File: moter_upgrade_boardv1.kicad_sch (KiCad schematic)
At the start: 54 parts, among them J2 Conn_01x03_Socket, J3 Conn_01x02_Socket, J4 Conn_01x02_Socket, J5 Conn_01x02_Socket, J6 Conn_01x02_Socket, J7 Conn_ST_STDC14, J8 Conn_01x05_Socket, J9 USB_C_Receptacle_USB2.0_16P, SW1 SW_SPDT, SW2 SW_Push, SW3 SW_Wuerth_450301014042, U1 BD33FC0FP, U2 TLP785, U3 TLP785, U4 STM32H523CCTx, U5 MCP2562-E-P, U6 CH340E, U7 BD33FC0FP

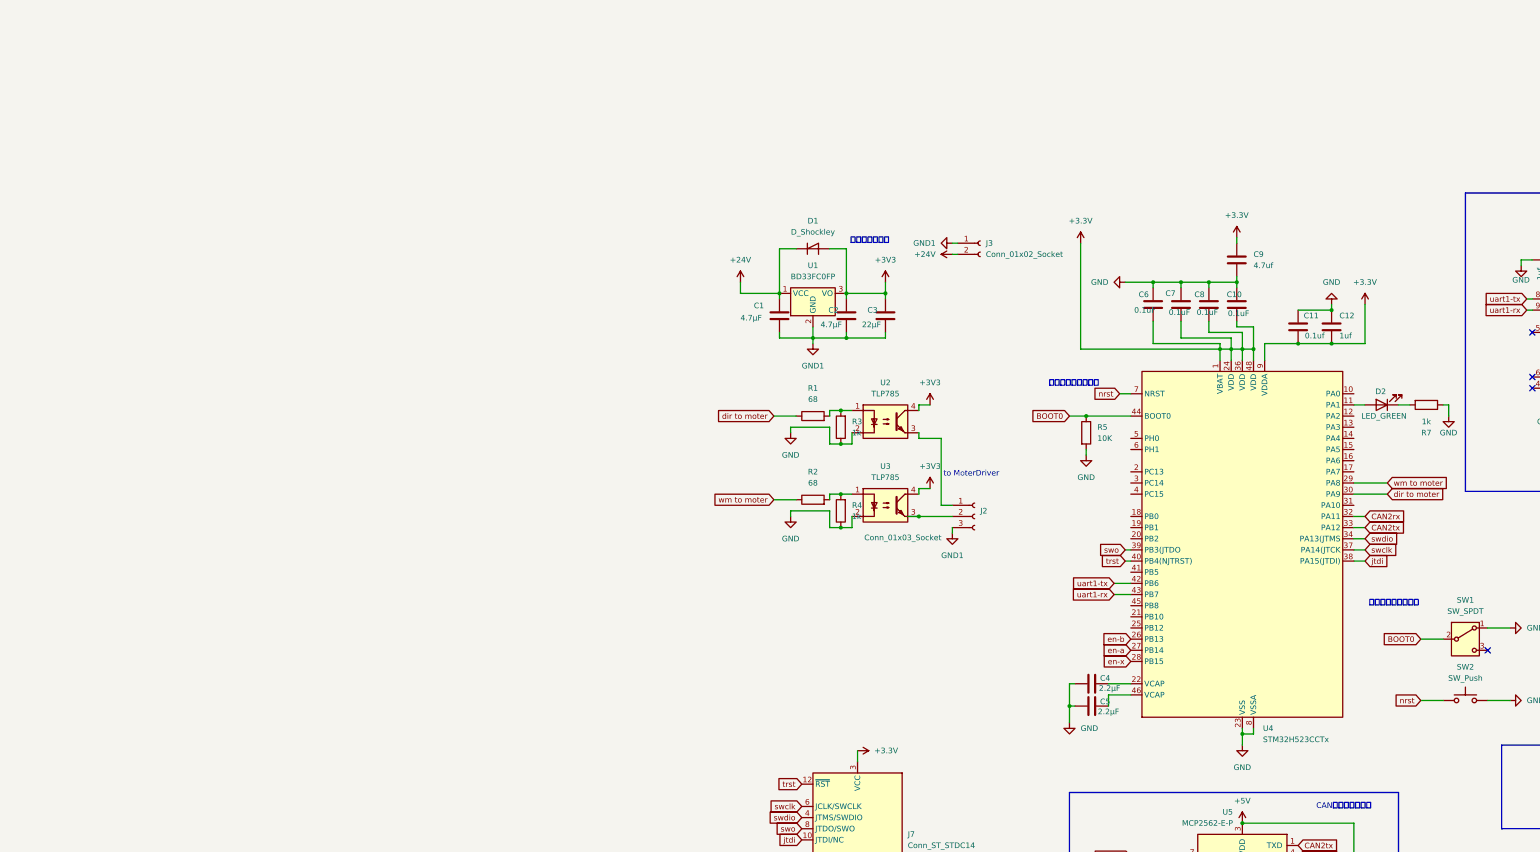
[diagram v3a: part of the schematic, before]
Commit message: マイコンの置き換え
stmH5からstmC5に置き換え(C5の中身はf446)
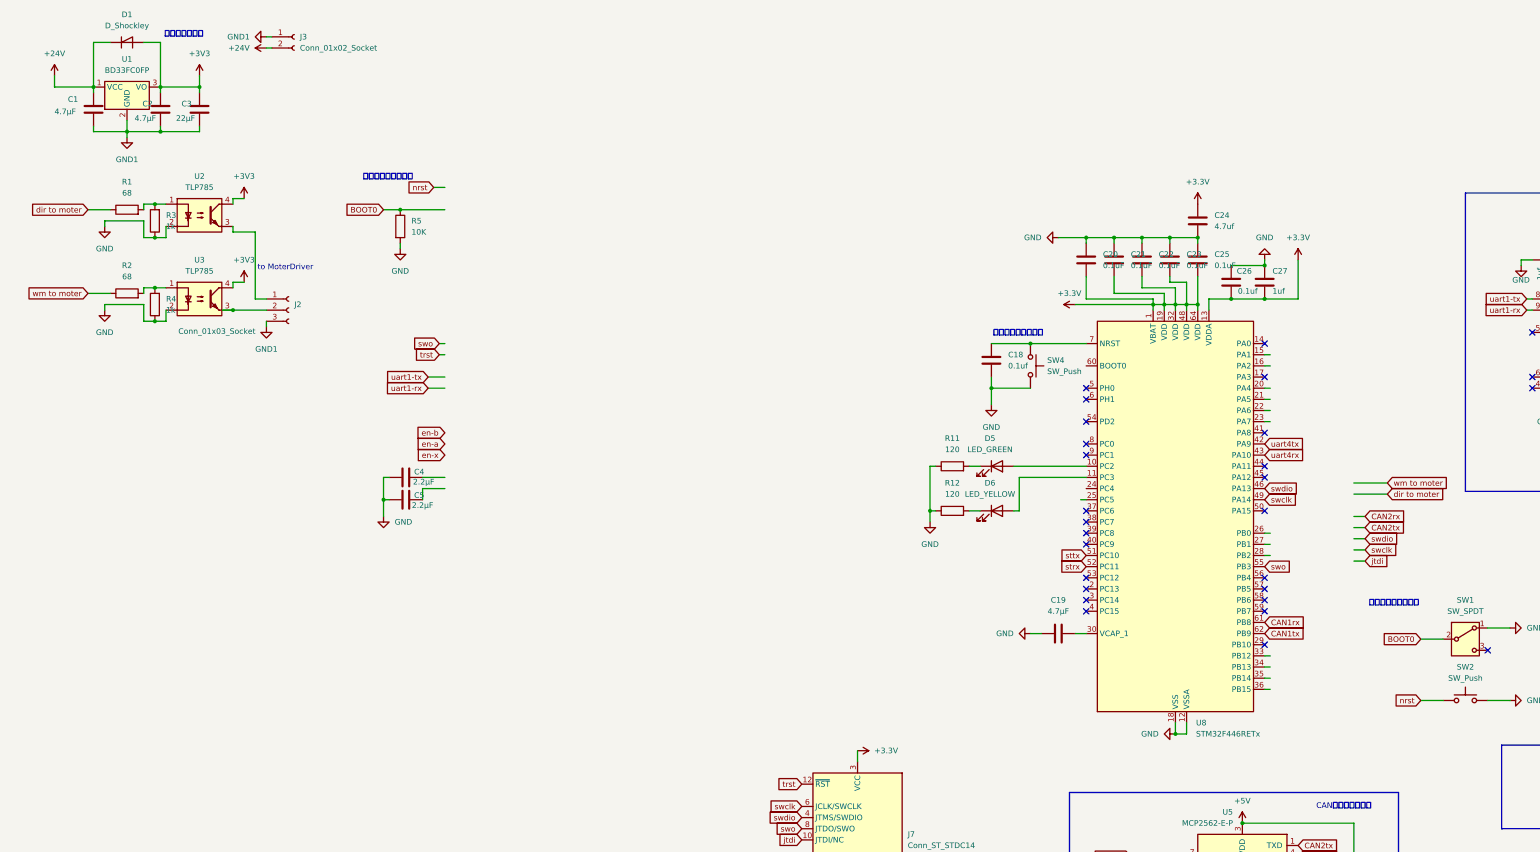
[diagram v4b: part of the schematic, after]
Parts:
- removed C10, C6, C7, C8: 0.1uF, Capacitor_SMD:C_0603_1608Metric_Pad1.08x0.95mm_HandSolder, symbol Device:C
- removed C11: 0.1uf, Capacitor_SMD:C_0603_1608Metric_Pad1.08x0.95mm_HandSolder, symbol Device:C
- removed C12: 1uf, Capacitor_SMD:C_0603_1608Metric_Pad1.08x0.95mm_HandSolder, symbol Device:C
- removed C9: 4.7uf, Capacitor_SMD:C_0805_2012Metric_Pad1.18x1.45mm_HandSolder, symbol Device:C
- removed D2: LED_GREEN, Capacitor_SMD:C_0603_1608Metric_Pad1.08x0.95mm_HandSolder, symbol Device:LED
- removed R7: 1k, Resistor_SMD:R_0603_1608Metric_Pad0.98x0.95mm_HandSolder, symbol Device:R
- removed U4: STM32H523CCTx, Package_QFP:LQFP-48_7x7mm_P0.5mm, symbol MCU_ST_STM32H5:STM32H523CCTx
- added C18: 0.1uf, Capacitor_SMD:C_0603_1608Metric_Pad1.08x0.95mm_HandSolder, symbol Device:C
- added C19: 4.7μF, Capacitor_SMD:C_0603_1608Metric_Pad1.08x0.95mm_HandSolder, symbol Device:C
- added C20, C21, C22, C23, C25: 0.1uF, Capacitor_SMD:C_0402_1005Metric_Pad0.74x0.62mm_HandSolder, symbol Device:C
- added C24: 4.7uf, Capacitor_SMD:C_0603_1608Metric_Pad1.08x0.95mm_HandSolder, symbol Device:C
- added C26: 0.1uf, Capacitor_SMD:C_0402_1005Metric_Pad0.74x0.62mm_HandSolder, symbol Device:C
- added C27: 1uf, Capacitor_SMD:C_0603_1608Metric_Pad1.08x0.95mm_HandSolder, symbol Device:C
- added D5: LED_GREEN, Diode_SMD:D_0805_2012Metric_Pad1.15x1.40mm_HandSolder, symbol Device:LED
- added D6: LED_YELLOW, Diode_SMD:D_0805_2012Metric_Pad1.15x1.40mm_HandSolder, symbol Device:LED
- added R11, R12: 120, Resistor_SMD:R_0603_1608Metric_Pad0.98x0.95mm_HandSolder, symbol Device:R
- added SW4: SW_Push, Button_Switch_THT:SW_PUSH_6mm, symbol Switch:SW_Push
- added U8: STM32F446RETx, Package_QFP:LQFP-64_10x10mm_P0.5mm, symbol MCU_ST_STM32F4:STM32F446RETx
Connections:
- net +3.3V: now also C20.1, C21.1, C22.1, C23.1, C24.1, C25.1, C26.2, C27.2, U8.1 (VBAT), U8.13 (VDDA), U8.19 (VDD), U8.32 (VDD), U8.48 (VDD), U8.64 (VDD)
- net GND: now also C18.2, C19.1, C20.2, C21.2, C22.2, C23.2, C24.2, C25.2, C26.1, C27.1, R11.1, R12.1, SW4.2, U8.12 (VSSA), U8.18 (VSS), U8.31 (VSS), U8.47 (VSS), U8.63 (VSS)
- net swclk: now also U8.49 (PA14)
- net swdio: now also U8.46 (PA13)
- net swo: now also U8.55 (PB3)
- new net: D6.1 (K), R12.2
- new net: C18.1, SW4.1, U8.7 (NRST)
- new net: D6.2 (A), U8.11 (PC3)
- new net: D5.1 (K), R11.2
- new net: D5.2 (A), U8.10 (PC2)
- new net: C19.2, U8.30 (VCAP_1)
- new net CAN1rx: U8.61 (PB8)
- new net CAN1tx: U8.62 (PB9)
- new net strx: U8.52 (PC11)
- new net sttx: U8.51 (PC10)
- new net uart4rx: U8.43 (PA10)
- new net uart4tx: U8.42 (PA9)
- no-connect marks 9 -> 33
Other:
- moved on the sheet: C1, C2, C3, C4, C5, D1, J2, J3, R1, R2, R3, R4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

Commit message: test
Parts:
- removed C14: 1uf, Capacitor_SMD:C_0603_1608Metric_Pad1.08x0.95mm_HandSolder, symbol Device:C
- removed C20: 0.1uF, Capacitor_SMD:C_0402_1005Metric_Pad0.74x0.62mm_HandSolder, symbol Device:C
- removed C4, C5: 2.2μF, Capacitor_SMD:C_0603_1608Metric_Pad1.08x0.95mm_HandSolder, symbol Device:C
- removed D5: LED_GREEN, Diode_SMD:D_0805_2012Metric_Pad1.15x1.40mm_HandSolder, symbol Device:LED
- removed J9: USB_C_Receptacle_USB2.0_16P, Connector_USB:USB_C_Receptacle_GCT_USB4105-xx-A_16P_TopMnt_Horizontal, symbol Connector:USB_C_Receptacle_USB2.0_16P
- removed R10, R9: 5.1k, Resistor_SMD:R_0603_1608Metric_Pad0.98x0.95mm_HandSolder, symbol Device:R
- removed R11: 120, Resistor_SMD:R_0603_1608Metric_Pad0.98x0.95mm_HandSolder, symbol Device:R
- removed SW2: SW_Push, Button_Switch_THT:SW_PUSH_6mm, symbol Switch:SW_Push
- removed U6: CH340E, Package_SO:MSOP-10_3x3mm_P0.5mm, symbol Interface_USB:CH340E
- added SW2: SW_SPDT, symbol Switch:SW_SPDT
- C21, C22, C23, C25, C26: footprint Capacitor_SMD:C_0402_1005Metric_Pad0.74x0.62mm_HandSolder -> Capacitor_SMD:C_0603_1608Metric
- C27: footprint Capacitor_SMD:C_0603_1608Metric_Pad1.08x0.95mm_HandSolder -> Capacitor_SMD:C_0603_1608Metric
- R12: value 120 -> 1k
- U8: value STM32F446RETx -> STM32C542CCT6
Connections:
- net trst is gone; now on net njtrst: J7.12 (~{RST})
- net +3.3V: no longer U8.1 (VBAT)
- net BOOT0: now also U8.60 (BOOT0)
- net CAN1rx: now also U8.33 (PB12); no longer U8.61 (PB8)
- net CAN1tx: now also U8.34 (PB13); no longer U8.62 (PB9)
- net CAN_H: now also J5.1 (Pin_1); no longer J5.2 (Pin_2)
- net CAN_L: now also J5.2 (Pin_2); no longer J5.1 (Pin_1)
- net dir to moter: now also U8.15 (PA1)
- net en-a: now also U8.3 (PC14)
- net en-b: now also U8.2 (PC13)
- net en-x: now also U8.4 (PC15)
- net jtdi: now also U8.50 (PA15)
- net strx: now also U8.59 (PB7); no longer U8.52 (PC11)
- net sttx: now also U8.58 (PB6); no longer U8.51 (PC10)
- net wm to moter: now also U8.16 (PA2)
- net njtrst: now reaches U8.56 (PB4)
- no-connect marks 33 -> 37
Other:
- note removed: "STlink,電源供給usbC"
- moved on the sheet: C1, C15, C16, C17, C18, C19, C2, C21, C22, C23, C24, C25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

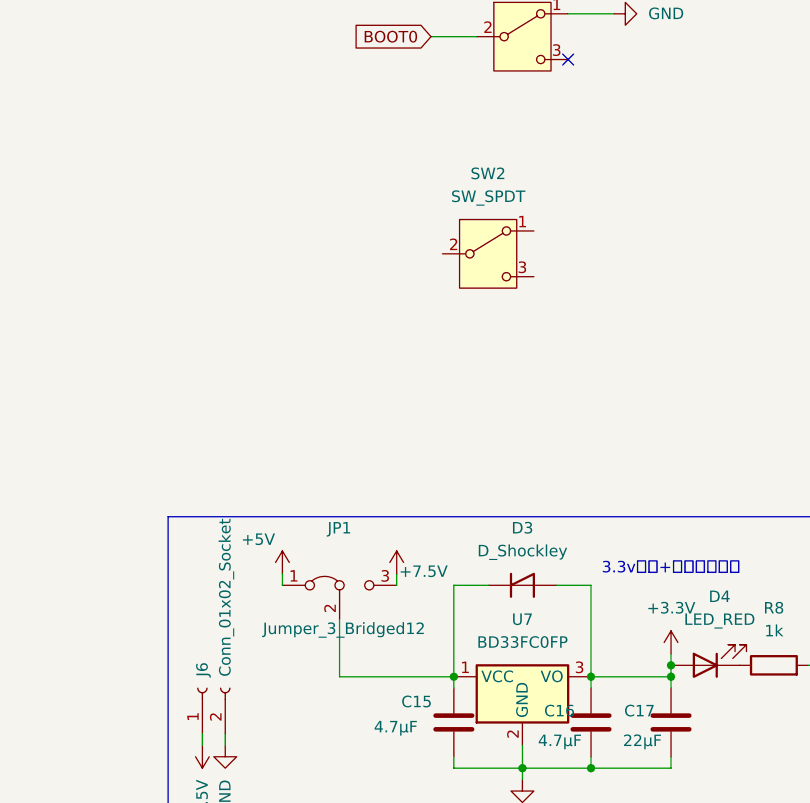
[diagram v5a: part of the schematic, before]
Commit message: 5v降圧レギュレーターの追加
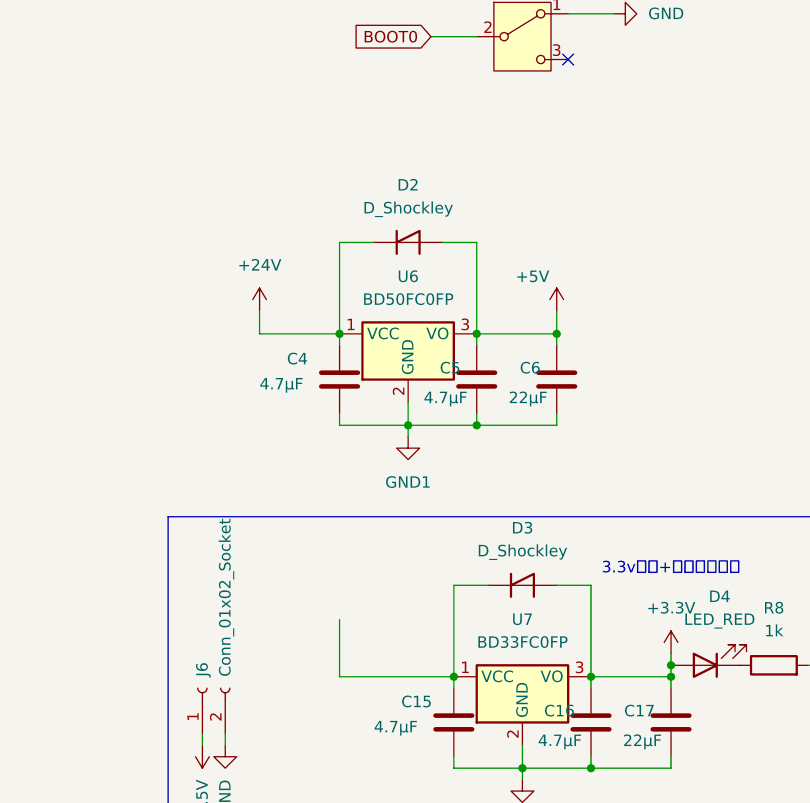
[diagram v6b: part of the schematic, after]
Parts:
- removed JP1: Jumper_3_Bridged12, Connector_PinSocket_2.54mm:PinSocket_1x03_P2.54mm_Vertical, symbol Jumper:Jumper_3_Bridged12
- removed SW2: SW_SPDT, symbol Switch:SW_SPDT
- added C4, C5: 4.7μF, Capacitor_SMD:C_0805_2012Metric_Pad1.18x1.45mm_HandSolder, symbol Device:C
- added C6: 22μF, Capacitor_SMD:C_0805_2012Metric_Pad1.18x1.45mm_HandSolder, symbol Device:C
- added D2: D_Shockley, Diode_SMD:D_SOD-323_HandSoldering, symbol Device:D_Shockley
- added U6: BD50FC0FP, Package_TO_SOT_SMD:TO-252-2, symbol Regulator_Linear:BD50FC0FP
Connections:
- net +24V: now also C4.1, D2.1 (K), U6.1 (VCC)
- net +5V: now also C5.1, C6.1, D2.2 (A), U6.3 (VO)
- net GND1: now also C4.2, C5.2, C6.2, U6.2 (GND)

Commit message: 一応
バックアップ的な感じ
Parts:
- removed C13: 0.1uf, Capacitor_SMD:C_0603_1608Metric_Pad1.08x0.95mm_HandSolder, symbol Device:C
- removed J4, J5: Conn_01x02_Socket, Connector_JST:JST_XH_S2B-XH-A-1_1x02_P2.50mm_Horizontal, symbol Connector:Conn_01x02_Socket
- removed R6: 120, Resistor_SMD:R_0603_1608Metric_Pad0.98x0.95mm_HandSolder, symbol Device:R
- removed SW3: SW_Wuerth_450301014042, Button_Switch_THT:SW_Slide-03_Wuerth-WS-SLTV_10x2.5x6.4_P2.54mm, symbol Switch:SW_Wuerth_450301014042
- removed U5: MCP2562-E-P, Package_DIP:DIP-8_W7.62mm, symbol Interface_CAN_LIN:MCP2562-E-P
- added C28: 0.1uF, Capacitor_SMD:C_0603_1608Metric_Pad1.08x0.95mm_HandSolder, symbol Device:C
- added C29: 4.7uF, Capacitor_SMD:C_0603_1608Metric_Pad1.08x0.95mm_HandSolder, symbol Device:C
- added J12, J13: Conn_01x02_Socket, Connector_JST:JST_XH_S2B-XH-A-1_1x02_P2.50mm_Horizontal, symbol Connector:Conn_01x02_Socket
- added R11: 120, Resistor_SMD:R_0603_1608Metric_Pad0.98x0.95mm_HandSolder, symbol Device:R
- added SW6: SW_Wuerth_450301014042, Button_Switch_THT:SW_Slide-03_Wuerth-WS-SLTV_10x2.5x6.4_P2.54mm, symbol Switch:SW_Wuerth_450301014042
- added U4: TCAN3414DRBR, TCAN3414DRBR:XCVR_TCAN3414DRBR, symbol TCAN3414DRBR:TCAN3414DRBR
- added U5: BD7F100HFN-LBTR, BD7:HSON8_ROM, symbol BD7:BD7F100HFN-LBTR
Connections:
- net +24V: now also U5.8 (VIN)
- net +3.3V: now also C28.2, C29.2, U4.3 (VCC)
- net CAN1rx: now also U4.4 (RXD)
- net CAN1tx: now also U4.1 (TXD)
- net GND: now also C28.1, C29.1, U4.2 (GND), U4.5 (SHDN), U4.8 (STB), U4.9 (EXP), U5.1 (AGND)
- net GND1: now also U5.6 (PGND)
- new net CAN1R: R11.2, SW6.3 (A)
- new net CAN1_H: J12.1 (Pin_1), J13.2 (Pin_2), R11.1, SW6.1 (B), U4.7 (CANH)
- new net CAN1_L: J12.2 (Pin_2), J13.1 (Pin_1), U4.6 (CANL)
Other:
- note removed: "CANトランシーバー"
- note removed: "終端抵抗オンオフ"
- moved on the sheet: C1, C18, C19, C2, C21, C22, C23, C24, C25, C26, C27, C3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
